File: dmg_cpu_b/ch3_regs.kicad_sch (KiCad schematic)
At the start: 115 parts

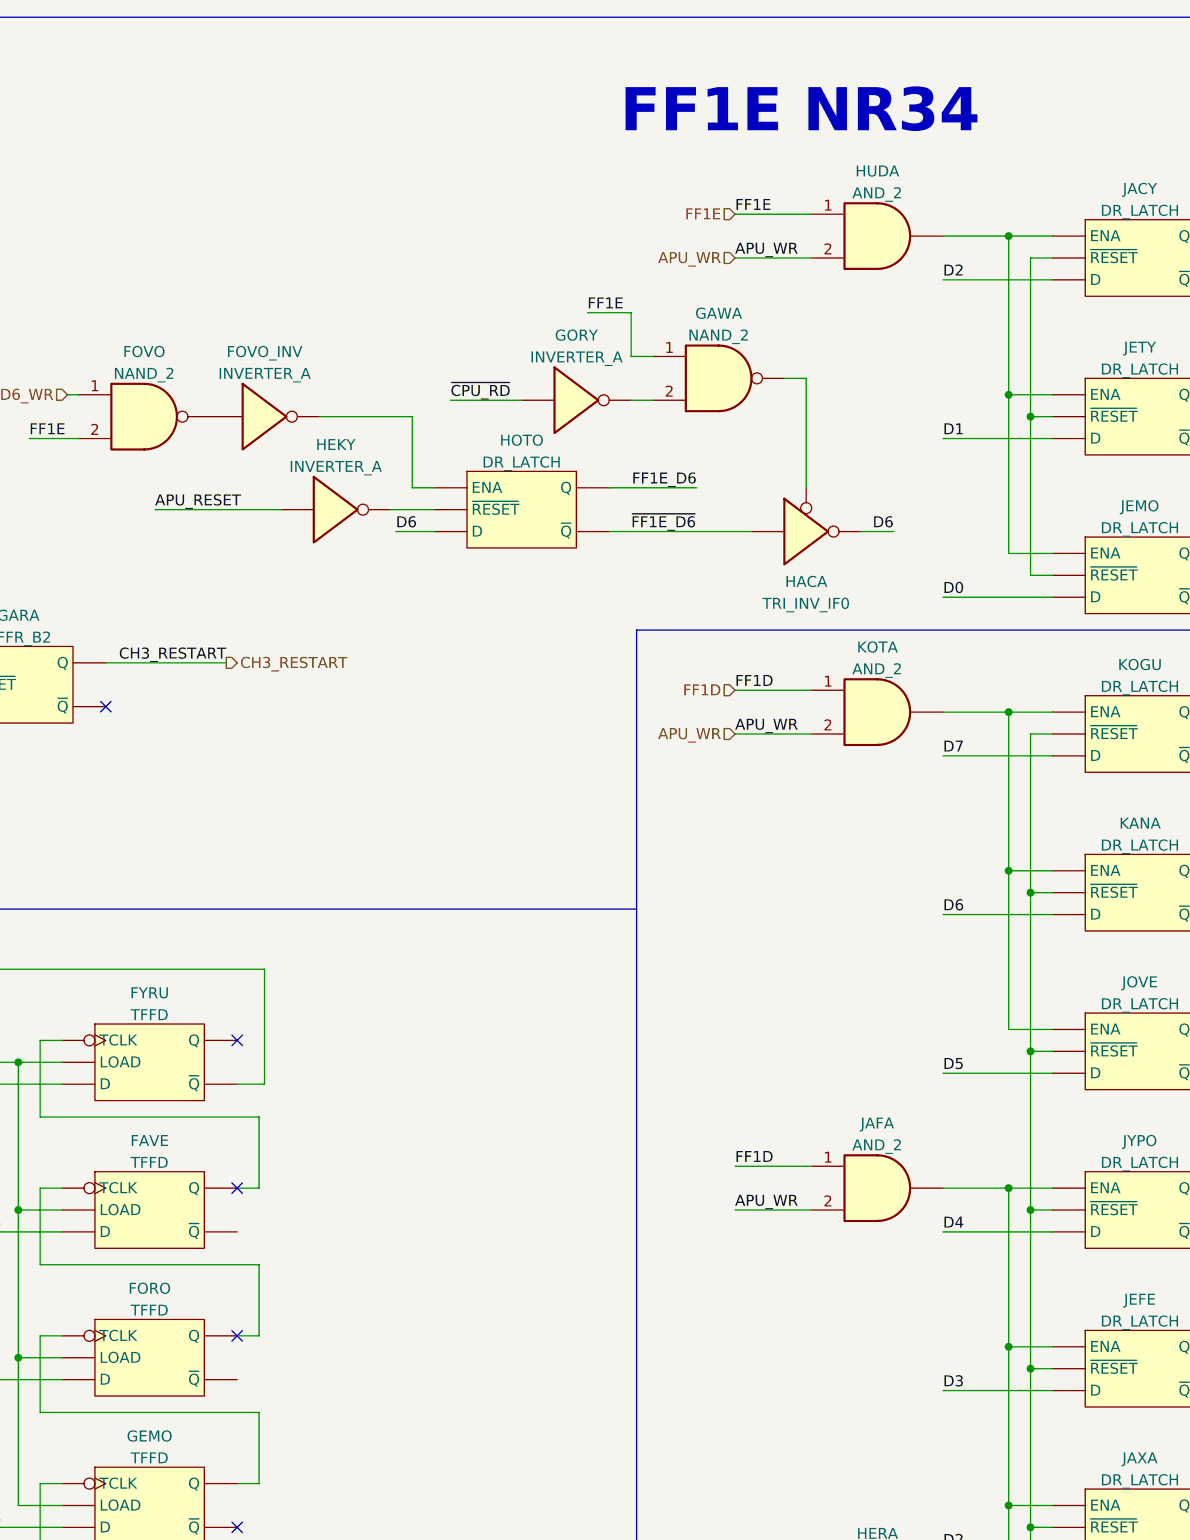
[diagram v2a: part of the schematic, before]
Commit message: Fixes made from issues, channel 4 sheet aded and tidy up of hierarchical APU sheet. Small fixes done here and there when doing ERC.
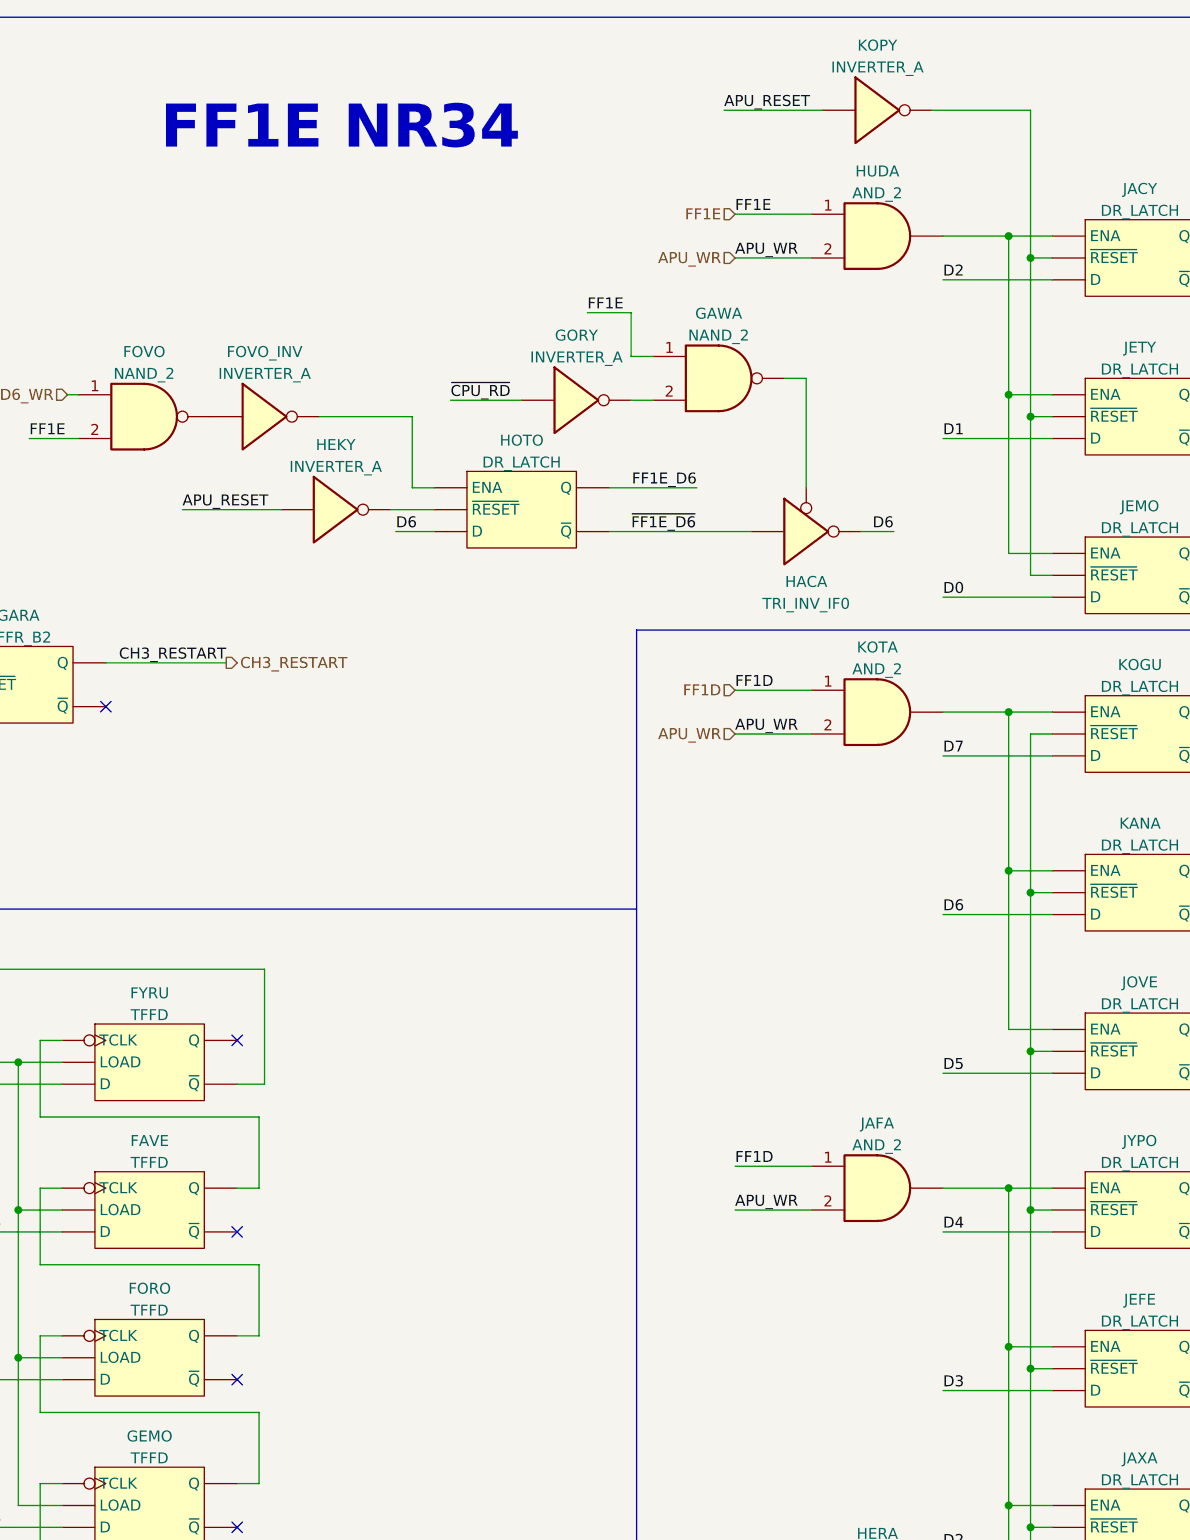
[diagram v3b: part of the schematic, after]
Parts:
- added KOPY: INVERTER_A, symbol DMG_CPU_Cells:INVERTER_A
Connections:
- net APU_RESET: now also KOPY.1
- net at JACY.4 (~{RESET}), JEMO.4 (~{RESET}), JETY.4 (~{RESET}): now also KOPY.2
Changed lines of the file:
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@@
   (junction (at 86.995 36.83) (diameter 0) (color 0 0 0 0)
+  )
+  (junction (at 287.02 41.275) (diameter 0) (color 0 0 0 0)
   )
   (junction (at 131.445 254.635) (diameter 0) (color 0 0 0 0)
@@
   (no_connect (at 118.745 110.49))
   (no_connect (at 194.945 222.885))
-  (no_connect (at 194.945 149.225))
+  (no_connect (at 194.945 154.305))
   (no_connect (at 144.145 93.345))
   (no_connect (at 110.49 67.31))
   (no_connect (at 194.945 240.03))
   (no_connect (at 80.645 123.19))
-  (no_connect (at 194.945 166.37))
+  (no_connect (at 194.945 171.45))
   (no_connect (at 309.88 43.815))
   (no_connect (at 82.55 67.31))
@@
     (stroke (width 0) (type default) (color 0 0 0 0))
   )
+  (wire (pts (xy 287.02 41.275) (xy 287.02 24.13))
+    (stroke (width 0) (type default) (color 0 0 0 0))
+  )
   (wire (pts (xy 377.19 122.555) (xy 377.19 125.73))
     (stroke (width 0) (type default) (color 0 0 0 0))
@@
     (stroke (width 0) (type default) (color 0 0 0 0))
   )
+  (wire (pts (xy 287.02 24.13) (xy 275.59 24.13))
+    (stroke (width 0) (type default) (color 0 0 0 0))
+  )
   (wire (pts (xy 317.5 49.53) (xy 322.58 49.53))
     (stroke (width 0) (type default) (color 0 0 0 0))
@@
     (stroke (width 0) (type default) (color 0 0 0 0))
   )
-  (wire (pts (xy 185.42 70.485) (xy 200.025 70.485))
+  (wire (pts (xy 188.595 70.485) (xy 200.025 70.485))
     (stroke (width 0) (type default) (color 0 0 0 0))
   )
@@
   )
   (wire (pts (xy 146.685 90.805) (xy 159.385 90.805))
+    (stroke (width 0) (type default) (color 0 0 0 0))
+  )
+  (wire (pts (xy 251.46 24.13) (xy 262.89 24.13))
     (stroke (width 0) (type default) (color 0 0 0 0))
   )
@@
     (effects (font (size 5 5) (thickness 0.8) bold) (justify left bottom))
   )
-  (text "FF1E NR34\n" (at 239.395 27.305 0)
+  (text "FF1E NR34\n" (at 186.055 29.21 0)
     (effects (font (size 5 5) (thickness 1) bold) (justify left bottom))
   )
@@
     (effects (font (size 1.27 1.27)) (justify left bottom))
   )
+  (label "APU_RESET" (at 251.46 24.13 0)
+    (effects (font (size 1.27 1.27)) (justify left bottom))
+  )
   (label "CH3_RESTART" (at 193.675 88.265 180)
     (effects (font (size 1.27 1.27)) (justify right bottom))
@@
     (effects (font (size 1.27 1.27)) (justify right bottom))
   )
-  (label "APU_RESET" (at 185.42 70.485 0)
+  (label "APU_RESET" (at 188.595 70.485 0)
     (effects (font (size 1.27 1.27)) (justify left bottom))
   )
@@
       (effects (font (size 1.27 1.27)) hide)
     )
+    (pin "1")
+    (pin "2")
+  )
+  (symbol (lib_id "DMG_CPU_Cells:INVERTER_A") (at 269.24 24.13 0) (unit 1)
+    (in_bom yes) (on_board yes)
+    (property "Reference" "KOPY" (id 0) (at 269.24 16.6202 0))
+    (property "Value" "INVERTER_A" (id 1) (at 269.24 19.1571 0))
+    (property "Footprint" "" (id 2) (at 266.7 24.13 0)
+      (effects (font (size 1.27 1.27)) hide)
+    )
+    (property "Datasheet" "http://iceboy.a-singer.de/doc/dmg_cells.html#inv_a" (id 3) (at 270.51 31.75 0)
+      (effects (font (size 1.27 1.27)) hide)
+    )

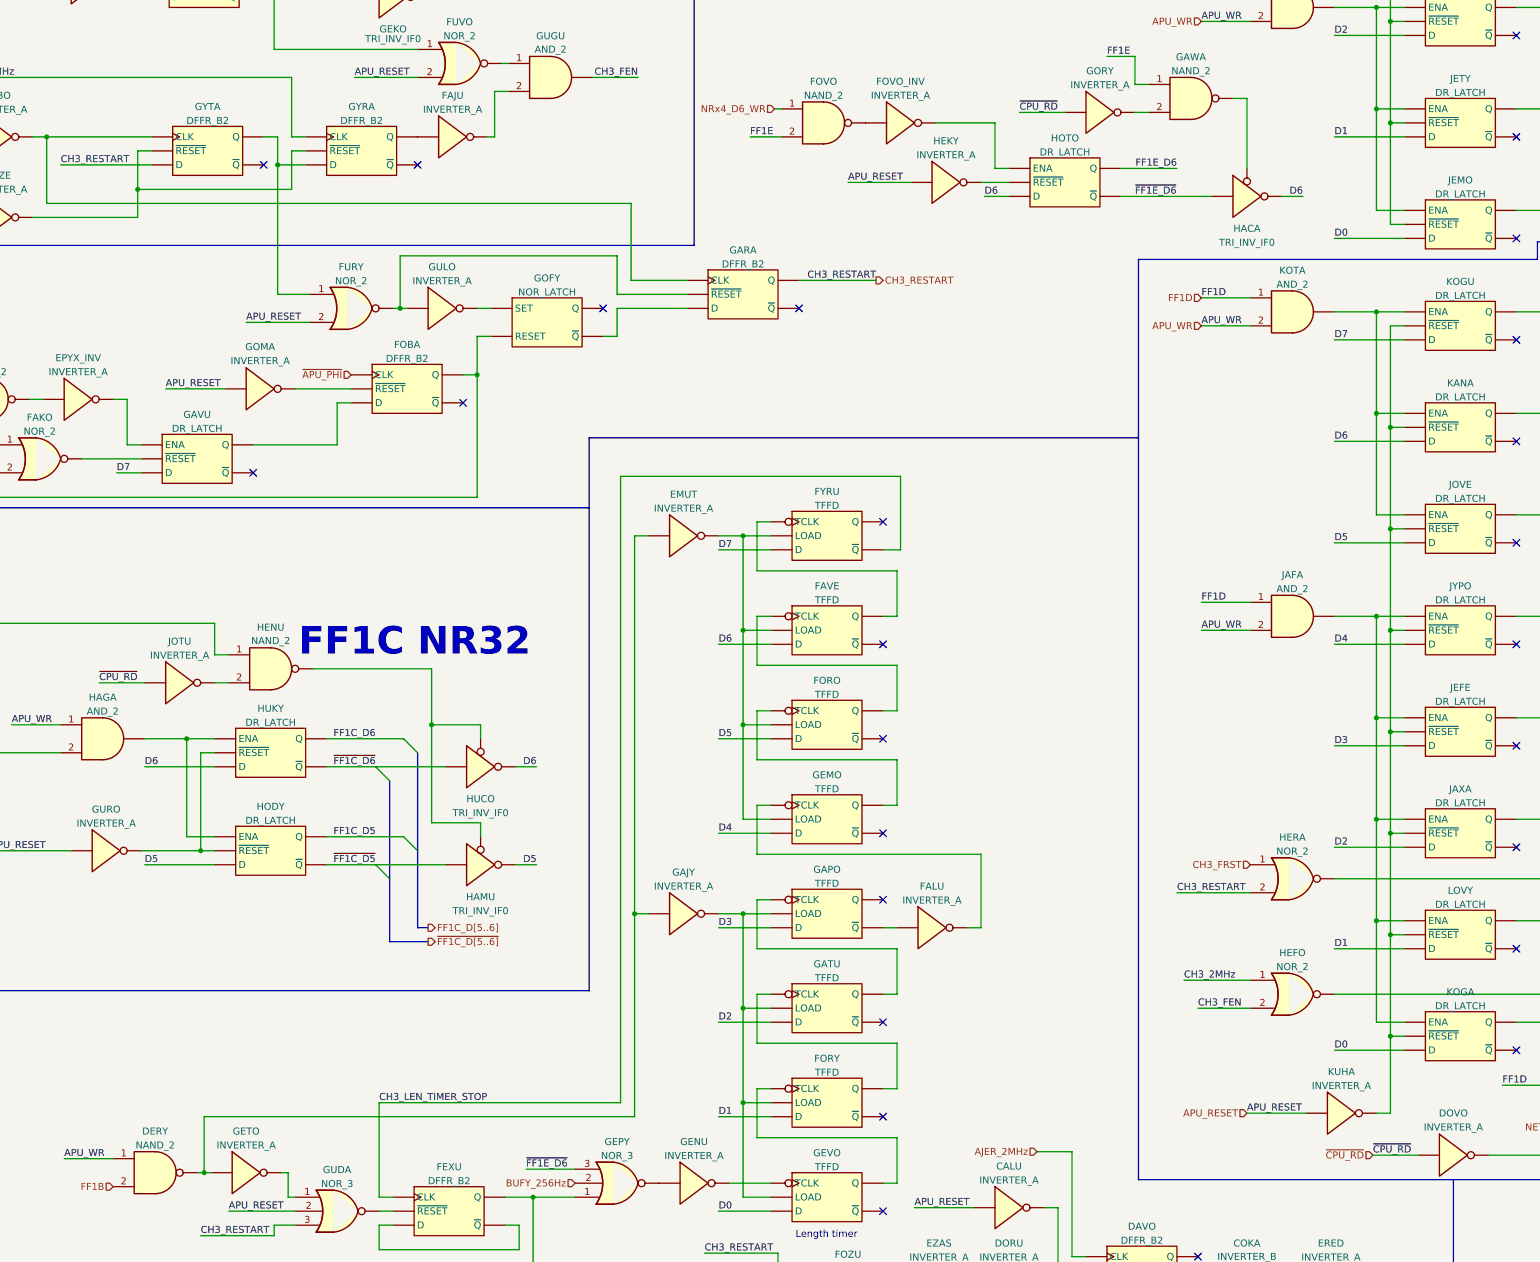
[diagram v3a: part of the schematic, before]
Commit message: Fixes made based on raised issues. PPU decode page added as draft level.
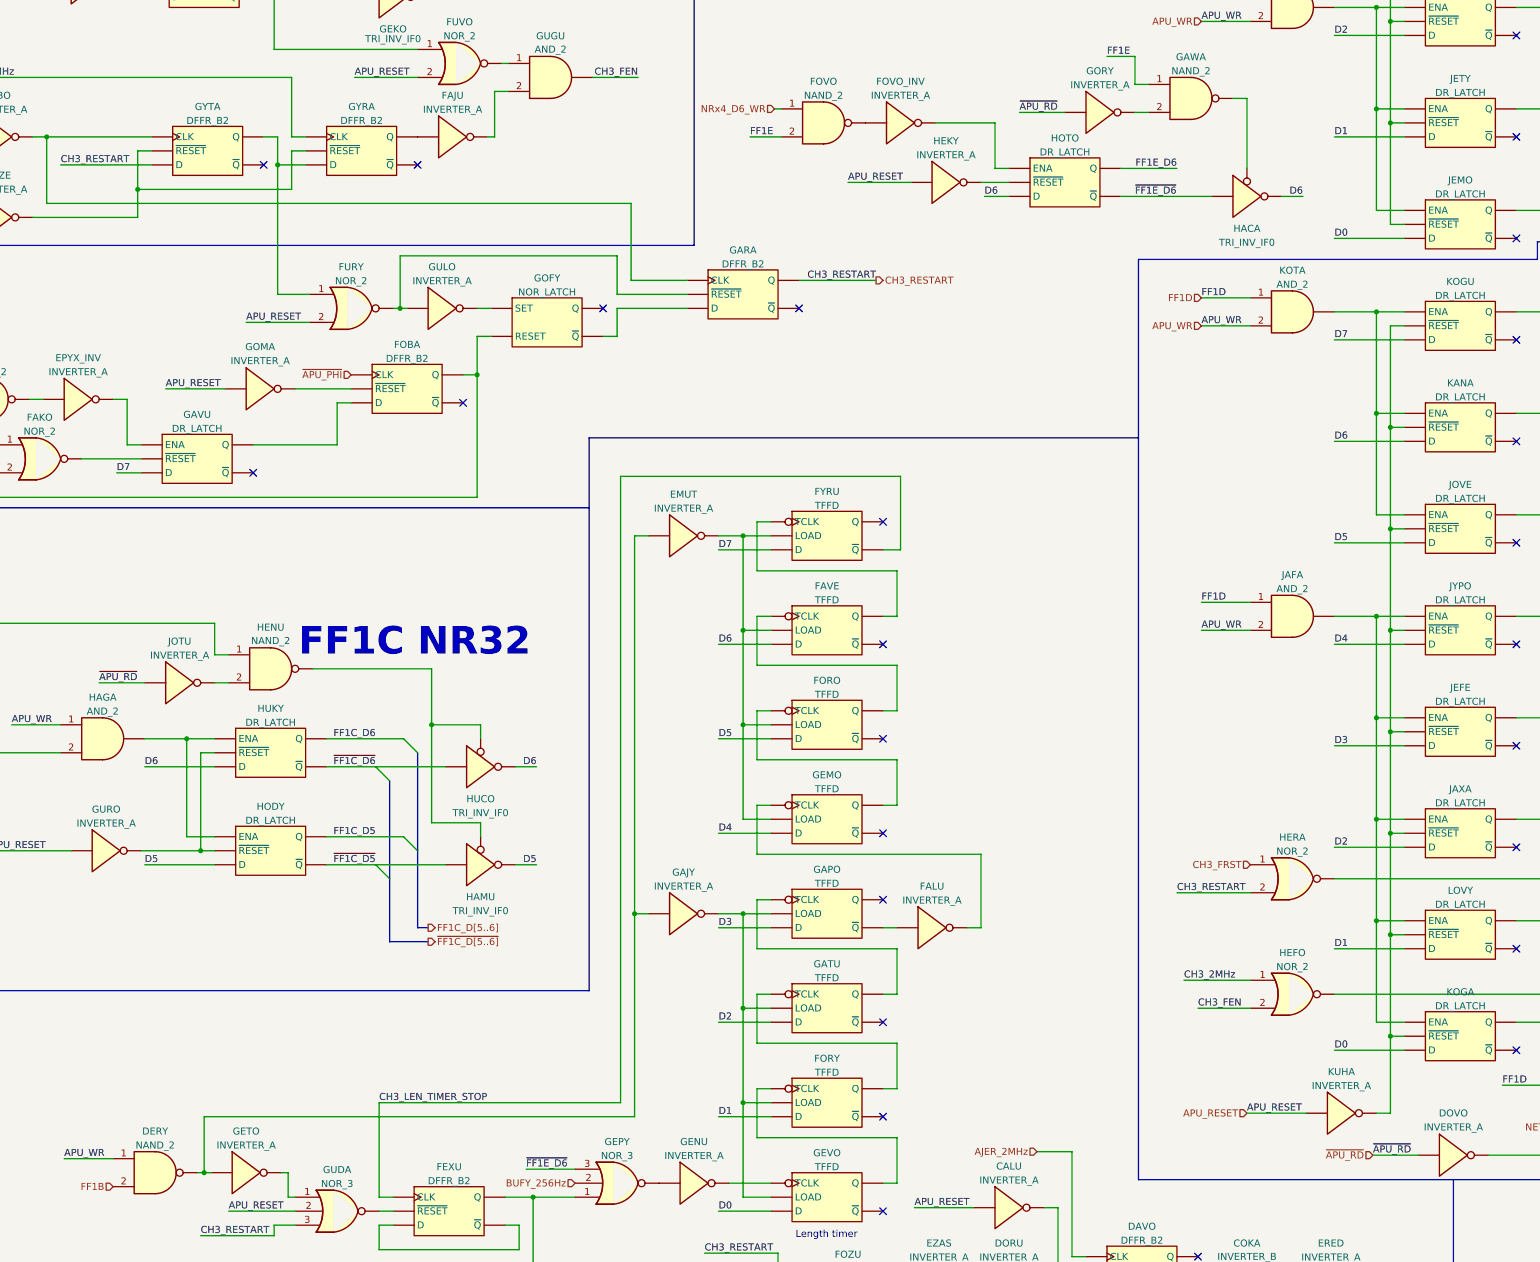
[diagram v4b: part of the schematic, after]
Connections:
- net ~{CPU_RD} renamed ~{APU_RD}
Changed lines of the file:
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@@
     (effects (font (size 1.27 1.27)) (justify left bottom))
   )
-  (label "~{CPU_RD}" (at 219.71 57.785 0)
+  (label "~{APU_RD}" (at 219.71 57.785 0)
     (effects (font (size 1.27 1.27)) (justify left bottom))
   )
@@
     (effects (font (size 1.27 1.27)) (justify left bottom))
   )
-  (label "~{CPU_RD}" (at 52.705 161.29 0)
+  (label "~{APU_RD}" (at 52.705 161.29 0)
     (effects (font (size 1.27 1.27)) (justify left bottom))
   )
@@
     (effects (font (size 1.27 1.27)) (justify left bottom))
   )
-  (label "~{CPU_RD}" (at 283.845 247.015 0)
+  (label "~{APU_RD}" (at 283.845 247.015 0)
     (effects (font (size 1.27 1.27)) (justify left bottom))
   )
@@
     (effects (font (size 1.27 1.27)) (justify right))
   )
-  (hierarchical_label "~{CPU_RD}" (shape input) (at 283.845 247.015 180)
+  (hierarchical_label "~{APU_RD}" (shape input) (at 283.845 247.015 180)
     (effects (font (size 1.27 1.27)) (justify right))
   )

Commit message: Further fixes made based on raised issues.
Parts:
- removed GUGU: AND_2, symbol DMG_CPU_Cells:AND_2
- added FEVO: INVERTER_A, symbol DMG_CPU_Cells:INVERTER_A
- added GUGU: NAND_LATCH, symbol DMG_CPU_Cells:NAND_LATCH
- renumbered LOVY to JOVY
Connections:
- net ~{CH3_AMP_EN}: now also FUVO.1; no longer GEKO.2
- net at GUXE.5 (Q): now also FEVO.1; no longer FUVO.1
- net at FUVO.3: now also GUGU.1 (~{RESET})
- net at FAJU.2: now also GUGU.4 (~{SET})
- net CH3_FEN renamed CH3_FDIS
- net CH3_FDIS: now also GUGU.3 (Q)
- new net: FEVO.2, GEKO.2
- no-connect marks 29 -> 30
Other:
- moved on the sheet: FABO, FAJU, FASY, FOVO, FOVO_INV, FUVO, GARA, GAWA, GAZE, GEKO, GORY, GYRA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

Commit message: Fixes made based on raised issues (in APU sheets).
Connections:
- net CH3_FDIS: now also GUGU.2 (~{Q}); no longer GUGU.3 (Q)
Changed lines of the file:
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@@
   (junction (at 287.02 188.595) (diameter 0) (color 0 0 0 0)
   )
-  (no_connect (at 149.86 54.61))
+  (no_connect (at 149.86 59.69))
   (no_connect (at 194.945 188.595))
   (no_connect (at 118.745 110.49))
@@
     (stroke (width 0) (type default) (color 0 0 0 0))
   )
-  (wire (pts (xy 158.75 59.69) (xy 149.86 59.69))
+  (wire (pts (xy 158.75 54.61) (xy 149.86 54.61))
     (stroke (width 0) (type default) (color 0 0 0 0))
   )
@@
     (effects (font (size 1.27 1.27)) (justify left bottom))
   )
-  (label "CH3_FDIS" (at 158.75 59.69 180)
+  (label "CH3_FDIS" (at 158.75 54.61 180)
     (effects (font (size 1.27 1.27)) (justify right bottom))
   )

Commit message: VRAM interface sheet added but various edits in existing sheets. Notable merge of RESET, CLOCKS and FF04 DIV sheets
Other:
- company: (none) -> CC-BY-SA-4.0 Régis Galland & Michael Singer -- Derived work from Furrtek
- title: (none) -> DMG CPU B
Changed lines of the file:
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@@
 (kicad_sch (version 20211123) (generator eeschema)
   (paper "A3")
+  (title_block
+    (title "DMG CPU B")
+    (date "2022-05-02")
+    (rev "0")
+    (company "CC-BY-SA-4.0 Régis Galland & Michael Singer -- Derived work from Furrtek")
+    (comment 1 "https://github.com/msinger/dmg-schematics")
+  )
   (junction (at 169.545 237.49) (diameter 0) (color 0 0 0 0)
   )
